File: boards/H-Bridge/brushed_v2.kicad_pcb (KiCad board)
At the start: 4 copper layers, 62 parts, among them IC1 ISO1042QDWVQ1, IC2 MIC4606-1YML-TR, IC3 AD8410AWBRZ-RL, IC4 TC1108-3.3VDBTR, J1 V+, J2 V-, J3 Motor-, J4 Motor+, J5 CANBus, J6 Encoder, J7 Prog_Header, J8 UART, J9 12V+, Q1 NTBLS4D0N15MC, Q2 NTBLS4D0N15MC, Q3 NTBLS4D0N15MC, Q4 NTBLS4D0N15MC, U1 STM32F103C8Tx, U2 LSF0102DCUR, U3 LSF0102DCUR

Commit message: Began proper FET layout/routing
need to fully define the copper layers, currently not well defined, also need to figure out how to get 12v to the gate driver
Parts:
- moved G*** 224.5 mm to (41.6, 39.8)
- moved J2 112.6 mm to (161.2, 141.5)
- moved C2 86.0 mm to (171.5, 115.2)
- moved C1 81.4 mm to (171.5, 104.5), turned to 180 degrees
- moved J1 80.8 mm to (161.2, 68.8)
- moved C8 79.4 mm to (175.5, 110.2), turned to 90 degrees
- moved J9 67.5 mm to (145.5, 68.8)
- moved R12 4.59 mm to (175.8, 119.5)
- moved U1 2.80 mm to (151.2, 103.8)
- moved R13 2.70 mm to (176.5, 101.5)
- moved R5 2.50 mm to (182.0, 91.8)
- moved D4 1.52 mm to (170.8, 101.5), turned to 180 degrees
- moved R8 1.15 mm to (180.8, 131.5)
- moved R7 1.00 mm to (197.2, 138.0)
- moved IC3 0.79 mm to (180.8, 123.0)
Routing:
- net Net-(IC2-ALO): track 16.4 -> 44.5 mm
- net /High Voltage&Sense/SHUNT+: track 0.00 -> 19.1 mm, vias 0 -> 46
- net /High Voltage&Sense/SHUNT-: track 0.00 -> 18.1 mm, vias 0 -> 11
- net /High Voltage&Sense/GATEB_HIGH: track 0.00 -> 5.49 mm
- net /High Voltage&Sense/GATEA_LOW: track 0.00 -> 4.26 mm
- net +3.3V: track 0.00 -> 2.84 mm
- net /MCU&Low_Voltage/SENSE: track 0.00 -> 1.85 mm, vias 0 -> 1
- net /High Voltage&Sense/GATEA_HIGH: track 13.9 -> 15.1 mm
- net /High Voltage&Sense/AHS: track 0.00 -> 1.14 mm
- net Net-(J3-Pin_1): vias 0 -> 36
- added copper zone on B.Cu, net /High Voltage&Sense/SHUNT+
- added copper zone on F.Cu, net /High Voltage&Sense/SHUNT+
- added copper zone on B.Cu, net /High Voltage&Sense/SHUNT-
- added copper zone on F.Cu, net /High Voltage&Sense/SHUNT-
- added copper zone on B.Cu, net Net-(J3-Pin_1)
- added copper zone on F.Cu, net Net-(J3-Pin_1)
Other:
- rule pad_to_mask_clearance: 0 -> 0.0635

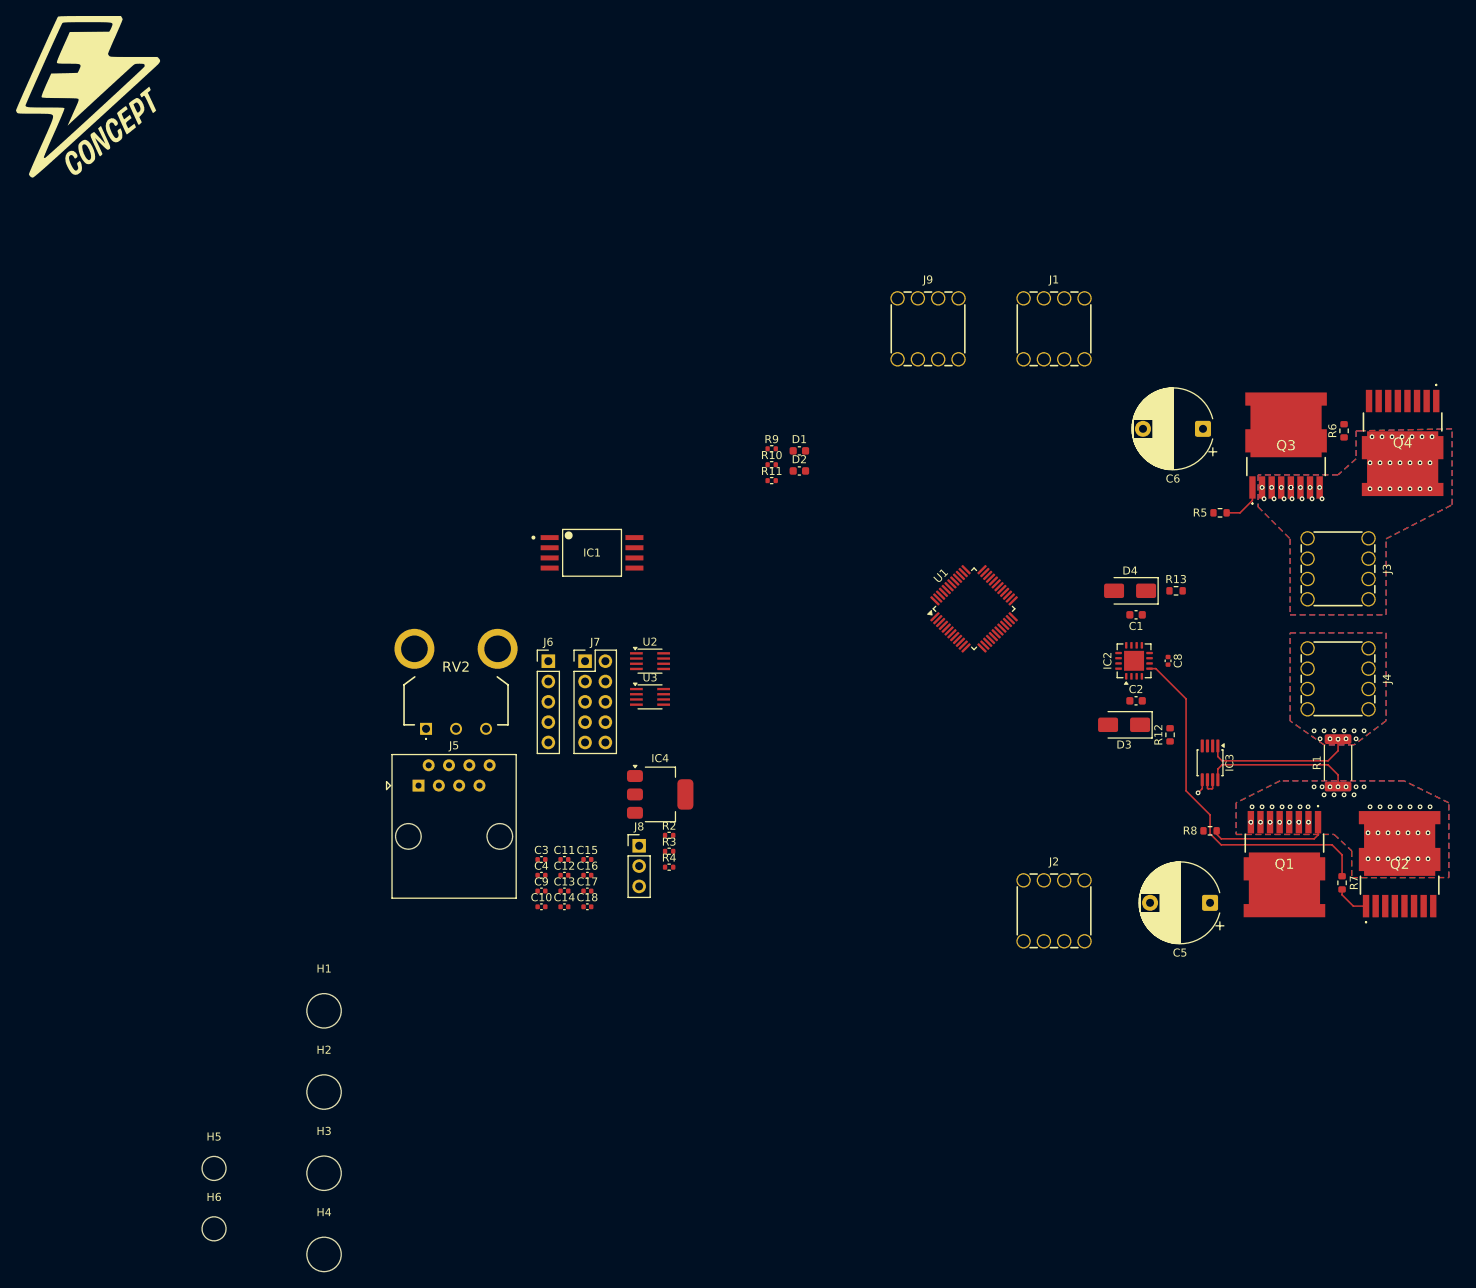
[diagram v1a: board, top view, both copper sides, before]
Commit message: finished layout, need to add silk key
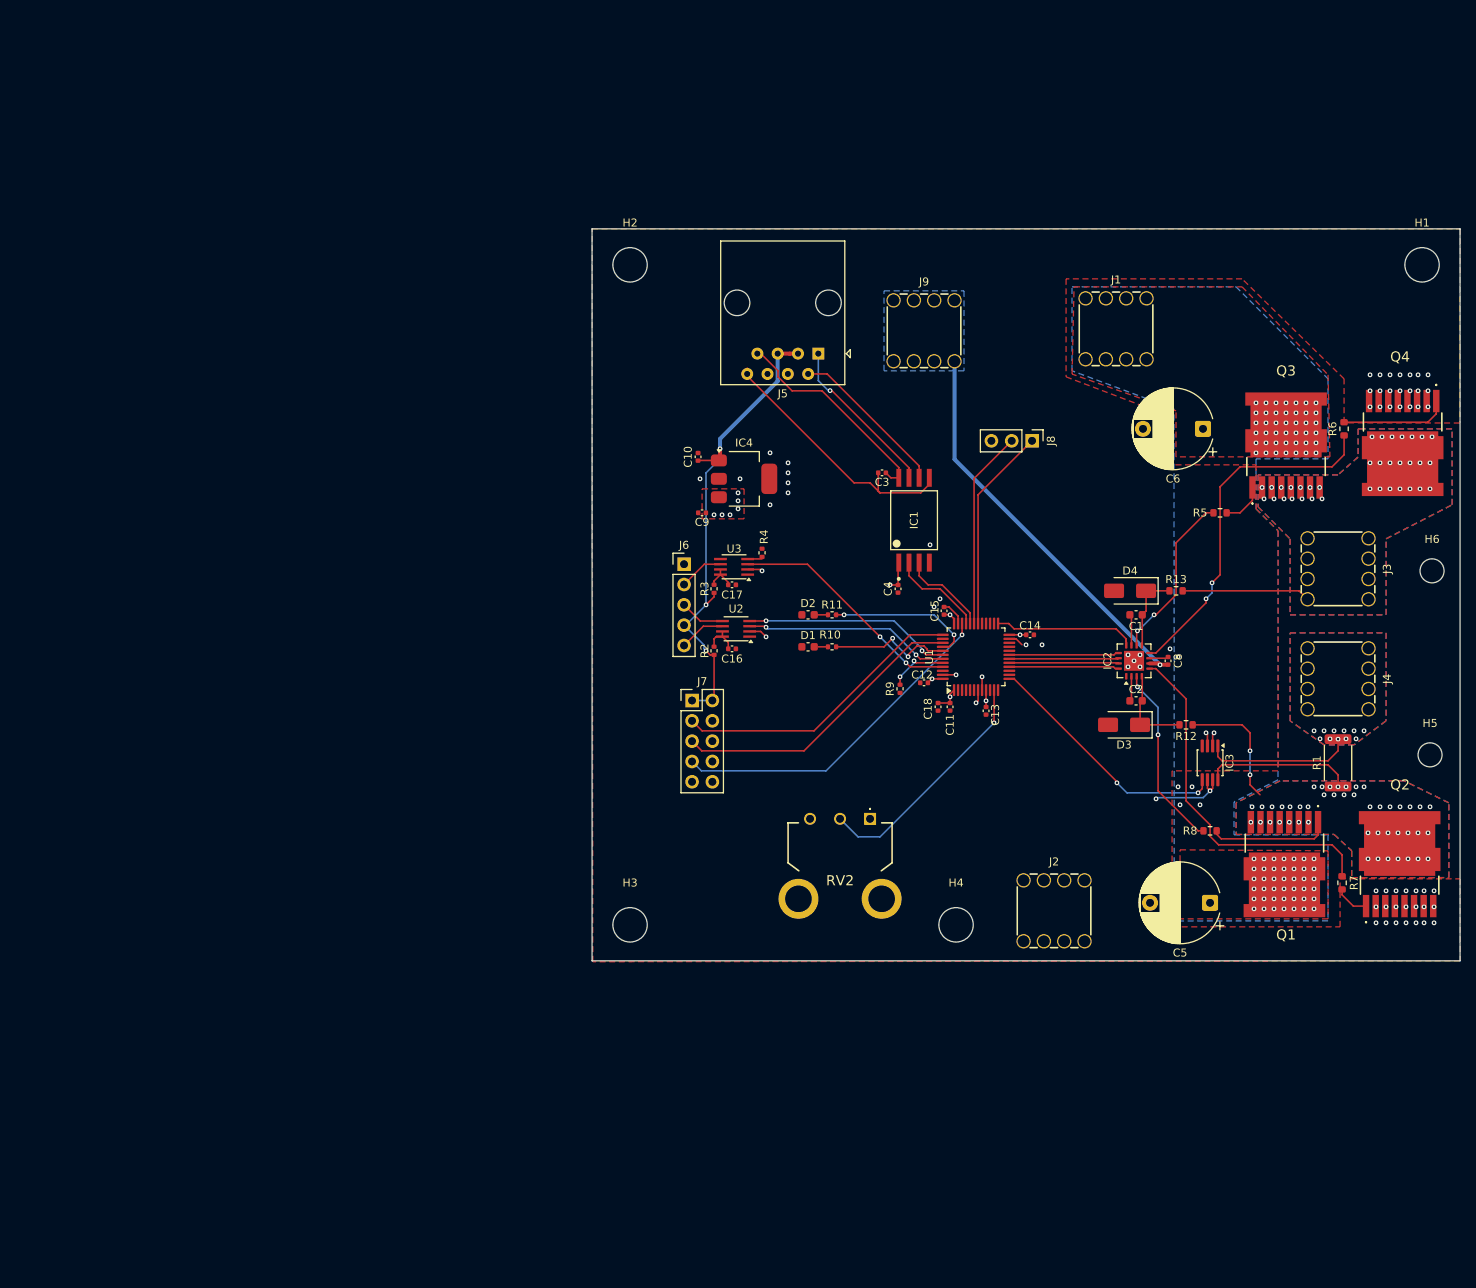
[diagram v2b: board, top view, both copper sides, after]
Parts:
- G***: moved to B.Cu
- moved H6 173.0 mm to (208.5, 99.0)
- moved H1 165.9 mm to (207.2, 60.8)
- moved H5 160.6 mm to (208.2, 122.0)
- moved G*** 134.3 mm to (163.9, 95.0), turned to 180 degrees
- moved H2 110.2 mm to (108.2, 60.8)
- moved H4 89.1 mm to (149.0, 143.2)
- moved J5 73.6 mm to (131.8, 71.8), turned to 180 degrees
- moved J8 70.5 mm to (158.5, 82.8), turned to -90 degrees
- moved C14 67.4 mm to (158.2, 107.0)
- moved C3 64.4 mm to (139.8, 86.8), turned to 180 degrees
- moved C10 59.6 mm to (116.8, 84.8), turned to 90 degrees
- moved C13 57.3 mm to (152.8, 116.5), turned to -90 degrees
- moved C4 57.2 mm to (141.8, 101.2), turned to -90 degrees
- moved RV2 56.6 mm to (138.2, 130.0), turned to 180 degrees
- moved C15 54.4 mm to (147.5, 104.0), turned to 90 degrees
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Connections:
- U1 pad 28: /MCU&Low_Voltage/IDX_3.3 -> unconnected-(U1-PB15-Pad28)
- U1 pad 45: unconnected-(U1-PB8-Pad45) -> /MCU&Low_Voltage/IDX_3.3
- U2 pad 3: /MCU&Low_Voltage/CHA_3.3 -> /MCU&Low_Voltage/CHB_3.3
- U2 pad 4: /MCU&Low_Voltage/CHB_3.3 -> /MCU&Low_Voltage/CHA_3.3
- U2 pad 5: /MCU&Low_Voltage/CH_B -> /MCU&Low_Voltage/CH_A
- U2 pad 6: /MCU&Low_Voltage/CH_A -> /MCU&Low_Voltage/CH_B
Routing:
- net +5V: track 0.00 -> 61.6 mm, vias 0 -> 3
- net +12V: track 0.00 -> 51.0 mm, vias 0 -> 1
- net Net-(IC2-BLO): track 0.00 -> 44.5 mm, vias 0 -> 2
- net /MCU&Low_Voltage/SWDIO: track 0.00 -> 42.7 mm, vias 0 -> 1
- net /MCU&Low_Voltage/SWO: track 0.00 -> 37.4 mm
- net /MCU&Low_Voltage/SWCLK: track 0.00 -> 36.8 mm
- net /MCU&Low_Voltage/CANGND: track 0.00 -> 33.7 mm
- net /MCU&Low_Voltage/POT_IN: track 0.00 -> 30.2 mm, vias 0 -> 1
- net /MCU&Low_Voltage/IDX_3.3: track 0.00 -> 29.7 mm, vias 0 -> 2
- net /MCU&Low_Voltage/SENSE: track 1.85 -> 31.4 mm, vias 1 -> 2
- net +3.3V: track 2.84 -> 31.6 mm, vias 0 -> 17
- net /MCU&Low_Voltage/CAN5V: track 0.00 -> 27.2 mm
- net /MCU&Low_Voltage/CHA_3.3: track 0.00 -> 26.1 mm, vias 0 -> 2
- net /MCU&Low_Voltage/CHB_3.3: track 0.00 -> 25.8 mm, vias 0 -> 2
- net /MCU&Low_Voltage/UART_TX: track 0.00 -> 25.6 mm
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- added copper zone on B.Cu, net +12V
- added copper zone on F.Cu, net +3.3V
- added copper zone on In2.Cu, net +3.3V
- added copper zone on B.Cu, net +48V
- added copper zone on F.Cu, net +48V
- added copper zone on In2.Cu, net +48V
- added copper zone on F.Cu, net GND
- added copper zone on In1.Cu, net GND
- added copper zone on In2.Cu, net GND
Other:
- board outline added: 108.5 x 91.5 mm

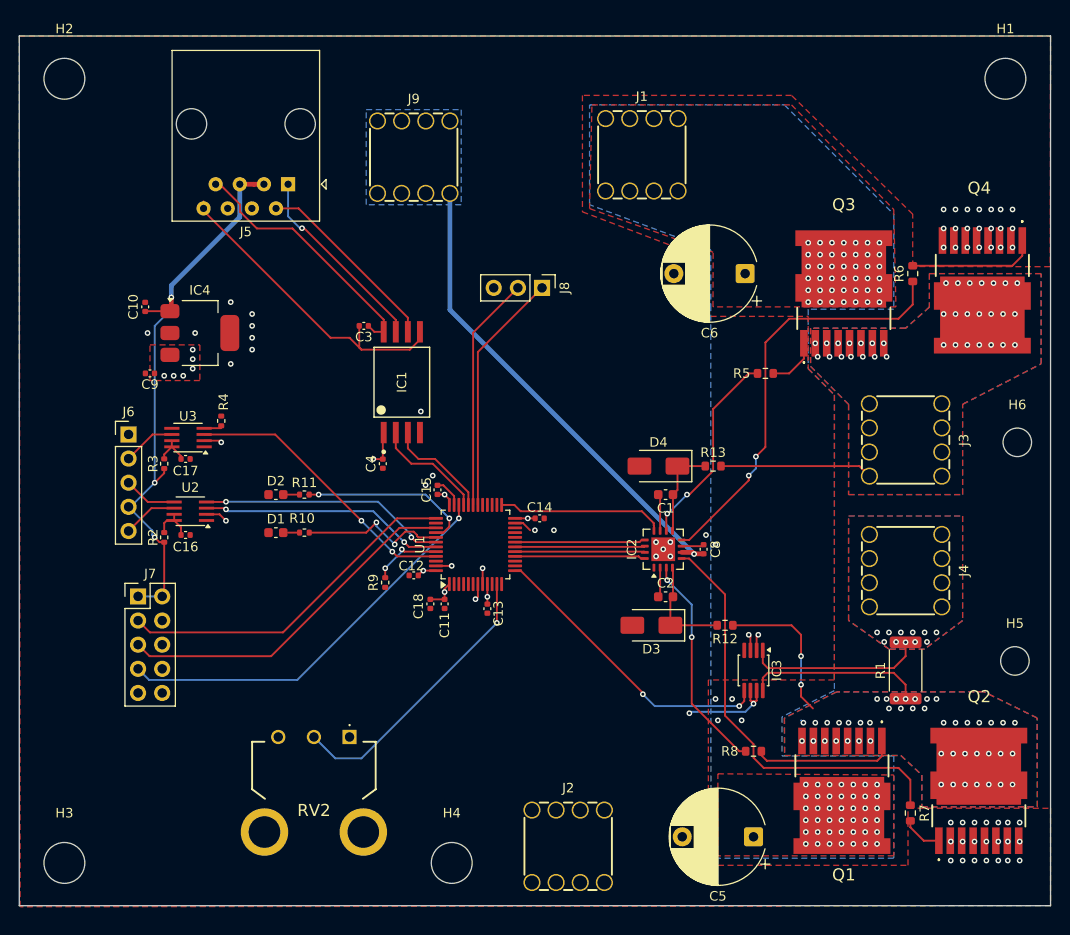
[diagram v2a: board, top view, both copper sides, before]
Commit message: made interactive BOM plus added via stich and labels
Jeremy
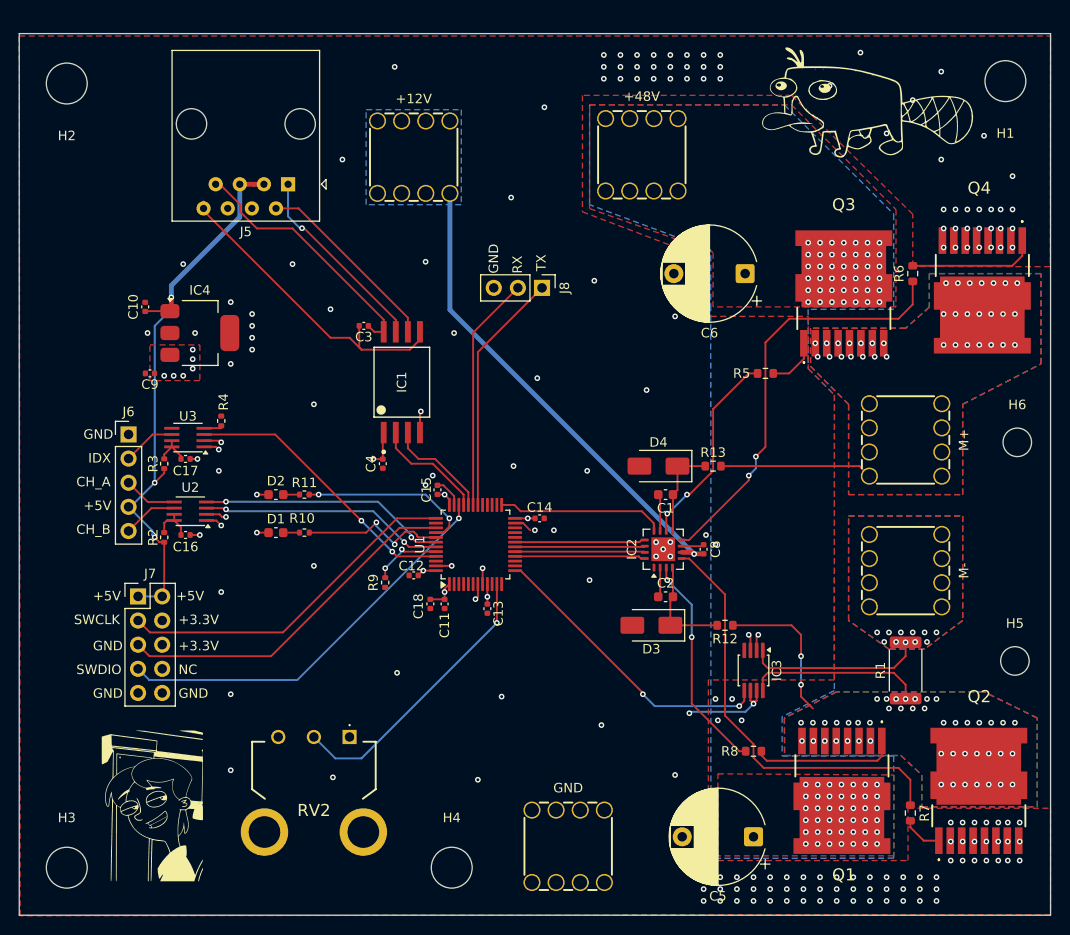
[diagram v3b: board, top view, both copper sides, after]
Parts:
- added G***: LOGO, EVC Logo:PERRY, F.Cu at (192.5, 65.4)
- added G***: LOGO, EVC Logo:Jeremy, F.Cu at (117.5, 137.2)
- added G***: LOGO, EVC Logo:Ferb, B.Cu at (119.5, 87.5)
- added G***: LOGO, EVC Logo:Phineas, B.Cu at (188.2, 67.2)
- moved H2 0.56 mm to (108.5, 61.2)
- moved H3 0.56 mm to (108.5, 143.8)
- moved H4 0.50 mm to (149.0, 143.8)
- moved H1 0.25 mm to (207.2, 61.0)
- renumbered J9 to +12V, J1 to +48V, J2 to GND, J3 to M+, J4 to M-
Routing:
- net GND: track 14.8 -> 24.7 mm, vias 66 -> 175
- net +3.3V: track 31.6 -> 31.5 mm, vias 17 -> 19
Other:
- board size 108.5 x 91.5 mm -> 108.5 x 92.8 mm
- board text added: "+3.3V"
- board text added: "+5V"
- board text added: "Brushed Motor Controller V2 (Jeremy) By: Ethan Rybka 2026/2027 SEM"
- board text added: "CH_A"
- board text added: "CH_B"
- board text added: "GND"
- board text added: "IDX"
- board text added: "NC"
- board text added: "RX"
- board text added: "SWCLK"
- board text added: "SWDIO"
- board text added: "TX"

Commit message: added another cursed silkscreen
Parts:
- added G***: LOGO, EVC Logo:holypeak, F.Cu at (183.5, 109.8)
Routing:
- net GND: vias 175 -> 169
- net +3.3V: vias 19 -> 25

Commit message: added dr doof
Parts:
- added G***: LOGO, EVC Logo:DOCTOR, B.Cu at (202.2, 133.0)
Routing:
- net GND: vias 169 -> 172
- net +3.3V: vias 25 -> 22
- added copper zone on In2.Cu, net /High Voltage&Sense/SHUNT+
- added copper zone on In2.Cu, net /High Voltage&Sense/SHUNT-
- added copper zone on In2.Cu, net Net-(J3-Pin_1)

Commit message: small changes
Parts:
- moved J5 1.50 mm to (131.8, 70.3)
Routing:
- net +5V: track 61.6 -> 63.1 mm
- net /MCU&Low_Voltage/CANH: track 20.5 -> 21.7 mm
- net /MCU&Low_Voltage/CANL: track 20.1 -> 21.2 mm
- net /MCU&Low_Voltage/CAN5V: track 27.2 -> 27.9 mm
- net /MCU&Low_Voltage/CANGND: track 33.7 -> 34.3 mm
- net GND: track 24.7 -> 24.4 mm, vias 172 -> 179
- net Net-(J3-Pin_1): vias 35 -> 42
- net /High Voltage&Sense/SHUNT+: vias 48 -> 55
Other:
- board text added: "Throttle Pot"
- board text added: "UART"

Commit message: fixed some pour stuff
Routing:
- net +3.3V: track 31.5 -> 33.3 mm
- net GND: vias 179 -> 172
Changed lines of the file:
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@@
 	)
 	(via
-		(at 206.5 76.5)
-		(size 0.6)
-		(drill 0.3)
-		(layers "F.Cu" "B.Cu")
-		(free yes)
-		(net "GND")
-	)
-	(via
 		(at 204.25 78.75)
 		(size 0.6)
@@
 	)
 	(via
-		(at 205.25 76.5)
-		(size 0.6)
-		(drill 0.3)
-		(layers "F.Cu" "B.Cu")
-		(free yes)
-		(net "GND")
-	)
-	(via
 		(at 184.25 146)
 		(size 0.6)
@@
 	)
 	(via
-		(at 202.75 76.5)
-		(size 0.6)
-		(drill 0.3)
-		(layers "F.Cu" "B.Cu")
-		(free yes)
-		(net "GND")
-	)
-	(via
 		(at 196.5 147.25)
 		(size 0.6)
@@
 	)
 	(via
-		(at 204 76.5)
-		(size 0.6)
-		(drill 0.3)
-		(layers "F.Cu" "B.Cu")
-		(free yes)
-		(net "GND")
-	)
-	(via
 		(at 207.5 141)
 		(size 0.6)
@@
 	)
 	(via
-		(at 201.5 76.5)
-		(size 0.6)
-		(drill 0.3)
-		(layers "F.Cu" "B.Cu")
-		(free yes)
-		(net "GND")
-	)
-	(via
 		(at 194.75 147.25)
 		(size 0.6)
@@
 	)
 	(via
-		(at 208.75 76.5)
-		(size 0.6)
-		(drill 0.3)
-		(layers "F.Cu" "B.Cu")
-		(free yes)
-		(net "GND")
-	)
-	(via
 		(at 191.25 147.25)
 		(size 0.6)
@@
 	)
 	(via
-		(at 207.5 76.5)
-		(size 0.6)
-		(drill 0.3)
-		(layers "F.Cu" "B.Cu")
-		(free yes)
-		(net "GND")
-	)
-	(via
 		(at 200.5 60)
 		(size 0.6)
@@
 	)
 	(segment
-		(start 122.95 98.825)
-		(end 124.575 98.825)
+		(start 148.25 115.52)
+		(end 146.75 115.52)
 		(width 0.2)
 		(layer "F.Cu")
@@
 	)
 	(segment
-		(start 148.25 115.52)
-		(end 146.75 115.52)
+		(start 157.77 107)
+		(end 157 107)
 		(width 0.2)
 		(layer "F.Cu")
@@
 	)
 	(segment
-		(start 157.77 107)
-		(end 157 107)
+		(start 124.575 98.825)
+		(end 122.95 98.825)
 		(width 0.2)
 		(layer "F.Cu")
@@
 	)
 	(segment
+		(start 124.850006 106.850006)
+		(end 124.575 106.575)
+		(width 0.2)
+		(layer "F.Cu")
+		(net "+3.3V")
+	)
+	(segment
+		(start 125.850006 106.850006)
+		(end 124.850006 106.850006)
+		(width 0.2)
+		(layer "F.Cu")
+		(net "+3.3V")
+	)
+	(segment
 		(start 148.25 115.52)
 		(end 148.25 114.75)
@@
 	)
 	(segment
-		(start 125.25 106.850006)
-		(end 124.850006 106.850006)
+		(start 126 107)
+		(end 125.850006 106.850006)
 		(width 0.2)
 		(layer "F.Cu")
@@
 	)
 	(segment
-		(start 124.575 98.825)
-		(end 124.75 99)
-		(width 0.2)
-		(layer "F.Cu")
-		(net "+3.3V")
-	)
-	(segment
 		(start 148.75 105.5875)
 		(end 148.75 105)
@@
 	)
 	(segment
-		(start 124.575 106.575)
-		(end 123.2 106.575)
+		(start 124.75 99)
+		(end 124.575 98.825)
 		(width 0.2)
 		(layer "F.Cu")
@@
 	)
 	(segment
+		(start 125.75 99)
+		(end 124.75 99)
+		(width 0.2)
+		(layer "F.Cu")
+		(net "+3.3V")
+	)
+	(segment
 		(start 146 112.5)
 		(end 145.98 112.5)
@@
 	)
 	(segment
-		(start 124.850006 106.850006)
-		(end 124.575 106.575)
+		(start 124.575 106.575)
+		(end 123.2 106.575)
 		(width 0.2)
 		(layer "F.Cu")
@@
 	)
 	(via
-		(at 125.25 106.850006)
+		(at 126 107)
 		(size 0.6)
 		(drill 0.3)
@@
 	)
 	(via
-		(at 124.75 99)
+		(at 125.75 99)
 		(size 0.6)
 		(drill 0.3)
@@
 	)
 	(zone
+		(layer "F.Cu")
+		(hatch edge 0.5)
+		(connect_pads
+			(clearance 0)
+		)
+		(min_thickness 0.25)
+		(keepout
+			(tracks allowed)
+			(vias allowed)
+			(pads allowed)
+			(copperpour not_allowed)
+			(footprints allowed)
+		)
+		(placement
+			(enabled no)
+			(sheetname "")
+		)
+		(fill
+			(thermal_gap 0.5)
+			(thermal_bridge_width 0.5)
+			(island_removal_mode 0)
+		)
+		(polygon
+			(pts
+				(xy 178.25 118.75) (xy 185.5 118.75) (xy 185.5 124) (xy 178.25 124)
+			)
+		)
+	)
+	(zone

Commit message: removed some copper islands
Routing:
- net GND: track 24.4 -> 29.8 mm, vias 172 -> 191
- net +3.3V: track 33.3 -> 33.8 mm, vias 22 -> 17
- net +48V: vias 88 -> 93
